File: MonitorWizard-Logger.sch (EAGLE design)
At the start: 40 parts, among them CON1 MICROSD, IC1 LD117AV33, J1 22-27-2041-04, J2 22-27-2041-04, J3 22-27-2041-04, U1 DHT22, U2 RFM69HW, U3 LTC3531, U4-NRF24L01 NRF24L01+-PCB-AERIAL, U6 ATMEGA328P-PU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

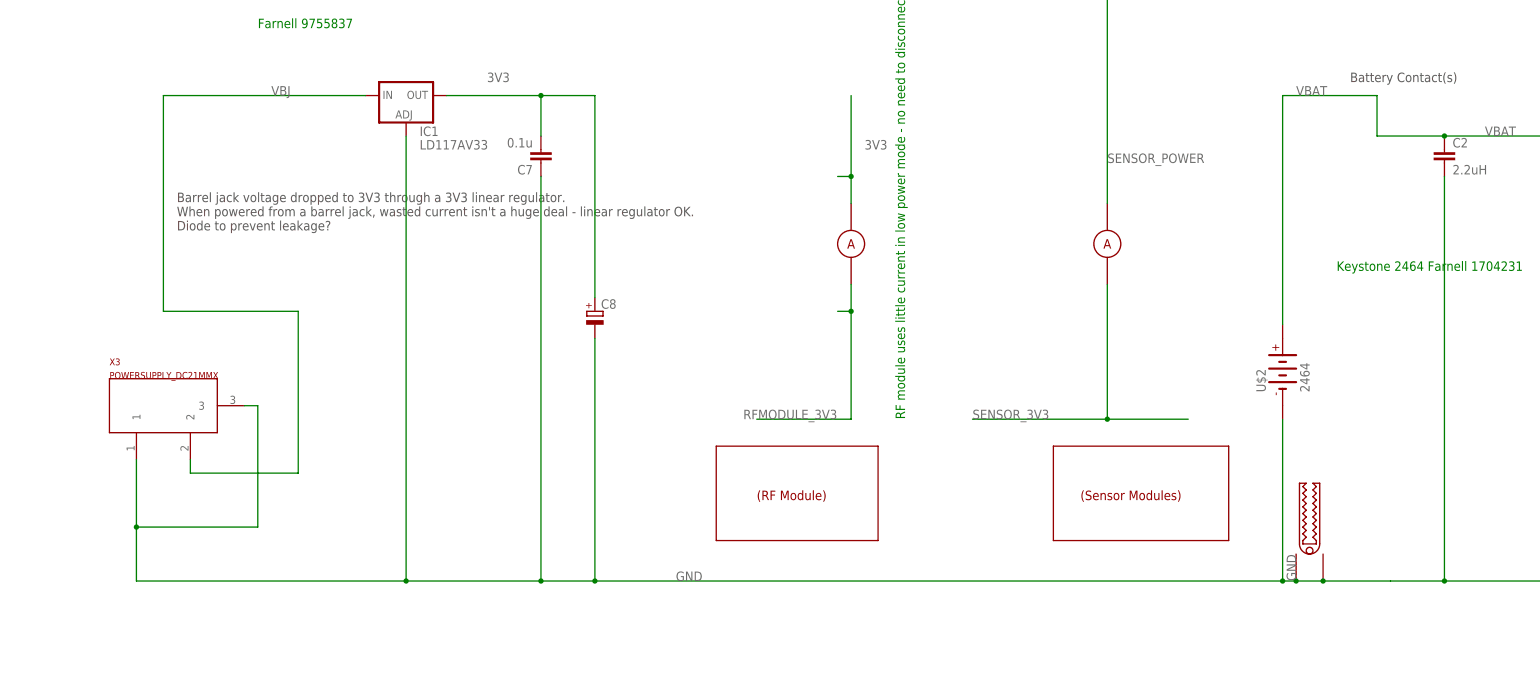
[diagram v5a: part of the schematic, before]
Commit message: Change to a better barrel jack footprint
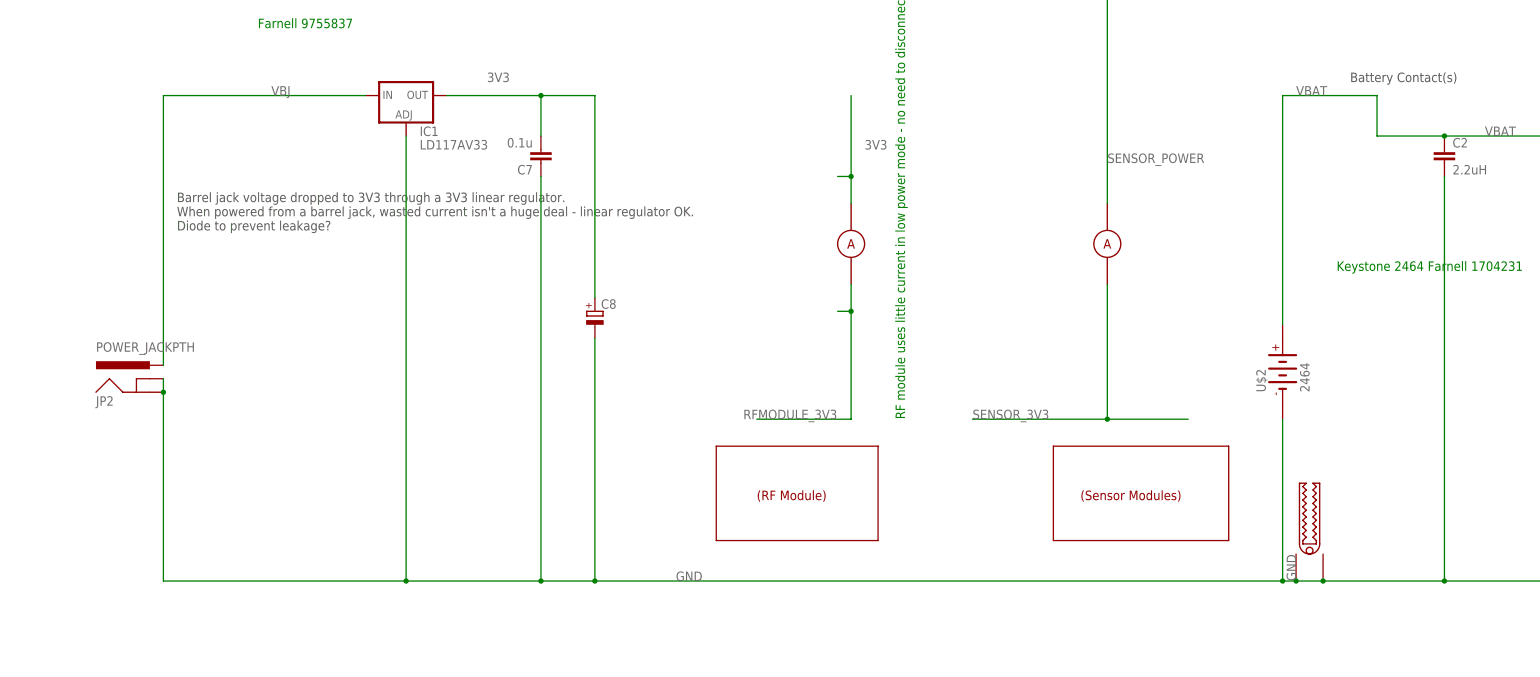
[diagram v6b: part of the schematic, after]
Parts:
- removed X3: POWERSUPPLY_DC21MMX, SmartPrj:POWERSUPPLY_DC21MMX
- added JP2: POWER_JACKPTH, SparkFun-Connectors:POWER_JACKPTH
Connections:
- net GND: now also JP2.GND, JP2.GNDBREAK; no longer X3.1, X3.3
- net VBJ: now also JP2.PWR; no longer X3.2
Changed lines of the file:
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@@
 <part name="AER" library="solpad" deviceset="LSP10" device=""/>
 <part name="GND" library="Probes" deviceset="ALLIGATOR" device=""/>
-<part name="X3" library="SmartPrj" deviceset="POWERSUPPLY_DC21MM" device="X"/>
 <part name="FD4" library="SmartPrj" deviceset="FIDUCIALMOUNT" device=""/>
 <part name="I_SENSE" library="Probes" deviceset="CURRENT_MEASURE" device="_0.4A"/>
@@
 <part name="C7" library="rcl" deviceset="C-EU" device="025-024X044" value="0.1u"/>
 <part name="C8" library="rcl" deviceset="CPOL-EU" device="E2.5-6"/>
+<part name="JP2" library="SparkFun-Connectors" deviceset="POWER_JACK" device="PTH"/>
 </parts>
 <sheets>
@@
 <instance part="AER" gate="1" x="408.94" y="-116.84" rot="R270"/>
 <instance part="GND" gate="G$1" x="525.78" y="-388.62" rot="R90"/>
-<instance part="X3" gate="G$1" x="309.88" y="-360.68" smashed="yes">
-<attribute name="NAME" x="299.72" y="-353.06" size="1.27" layer="94"/>
-<attribute name="VALUE" x="299.72" y="-355.6" size="1.27" layer="94"/>
-</instance>
 <instance part="FD4" gate="G$1" x="599.44" y="-88.9"/>
 <instance part="I_SENSE" gate="G$1" x="487.68" y="-330.2"/>
@@
 <instance part="C7" gate="G$1" x="381" y="-314.96" rot="R180"/>
 <instance part="C8" gate="G$1" x="391.16" y="-342.9"/>
+<instance part="JP2" gate="G$1" x="307.34" y="-360.68"/>
 </instances>
 <busses>
@@
 <net name="GND" class="2">
 <segment>
-<wire x1="528.32" y1="-393.7" x2="541.02" y2="-393.7" width="0.1524" layer="91"/>
+<wire x1="528.32" y1="-393.7" x2="551.18" y2="-393.7" width="0.1524" layer="91"/>
 <label x="406.4" y="-393.7" size="1.778" layer="95"/>
 <pinref part="GND" gate="G$1" pin="TOP"/>
@@
 <pinref part="GND" gate="G$1" pin="BTM"/>
 <junction x="528.32" y="-393.7"/>
-<pinref part="X3" gate="G$1" pin="3"/>
-<wire x1="325.12" y1="-360.68" x2="327.66" y2="-360.68" width="0.1524" layer="91"/>
-<wire x1="327.66" y1="-360.68" x2="327.66" y2="-383.54" width="0.1524" layer="91"/>
-<pinref part="X3" gate="G$1" pin="1"/>
-<wire x1="327.66" y1="-383.54" x2="304.8" y2="-383.54" width="0.1524" layer="91"/>
-<wire x1="304.8" y1="-383.54" x2="304.8" y2="-370.84" width="0.1524" layer="91"/>
-<wire x1="304.8" y1="-383.54" x2="304.8" y2="-393.7" width="0.1524" layer="91"/>
-<wire x1="304.8" y1="-393.7" x2="355.6" y2="-393.7" width="0.1524" layer="91"/>
-<junction x="304.8" y="-383.54"/>
+<wire x1="309.88" y1="-393.7" x2="355.6" y2="-393.7" width="0.1524" layer="91"/>
 <wire x1="355.6" y1="-393.7" x2="381" y2="-393.7" width="0.1524" layer="91"/>
 <wire x1="381" y1="-393.7" x2="391.16" y2="-393.7" width="0.1524" layer="91"/>
@@
 <wire x1="586.74" y1="-393.7" x2="551.18" y2="-393.7" width="0.1524" layer="91"/>
 <pinref part="R1" gate="G$1" pin="1"/>
-<wire x1="551.18" y1="-393.7" x2="541.02" y2="-393.7" width="0.1524" layer="91"/>
 <wire x1="612.14" y1="-373.38" x2="612.14" y2="-393.7" width="0.1524" layer="91"/>
 <wire x1="612.14" y1="-393.7" x2="586.74" y2="-393.7" width="0.1524" layer="91"/>
@@
 <wire x1="391.16" y1="-347.98" x2="391.16" y2="-393.7" width="0.1524" layer="91"/>
 <junction x="391.16" y="-393.7"/>
+<pinref part="JP2" gate="G$1" pin="GNDBREAK"/>
+<pinref part="JP2" gate="G$1" pin="GND"/>
+<wire x1="309.88" y1="-355.6" x2="309.88" y2="-358.14" width="0.1524" layer="91"/>
+<wire x1="309.88" y1="-358.14" x2="309.88" y2="-393.7" width="0.1524" layer="91"/>
+<junction x="309.88" y="-358.14"/>
 </segment>
 <segment>
@@
 <net name="VBJ" class="0">
 <segment>
-<pinref part="X3" gate="G$1" pin="2"/>
-<wire x1="314.96" y1="-370.84" x2="314.96" y2="-373.38" width="0.1524" layer="91"/>
-<wire x1="314.96" y1="-373.38" x2="335.28" y2="-373.38" width="0.1524" layer="91"/>
 <label x="330.2" y="-302.26" size="1.778" layer="95"/>
-<wire x1="335.28" y1="-373.38" x2="335.28" y2="-342.9" width="0.1524" layer="91"/>
-<wire x1="335.28" y1="-342.9" x2="309.88" y2="-342.9" width="0.1524" layer="91"/>
-<wire x1="309.88" y1="-342.9" x2="309.88" y2="-302.26" width="0.1524" layer="91"/>
+<wire x1="309.88" y1="-353.06" x2="309.88" y2="-302.26" width="0.1524" layer="91"/>
 <wire x1="309.88" y1="-302.26" x2="347.98" y2="-302.26" width="0.1524" layer="91"/>
 <pinref part="IC1" gate="G$1" pin="IN"/>
-</segment>
-</net>
+<pinref part="JP2" gate="G$1" pin="PWR"/>
+</segment>
+</net>

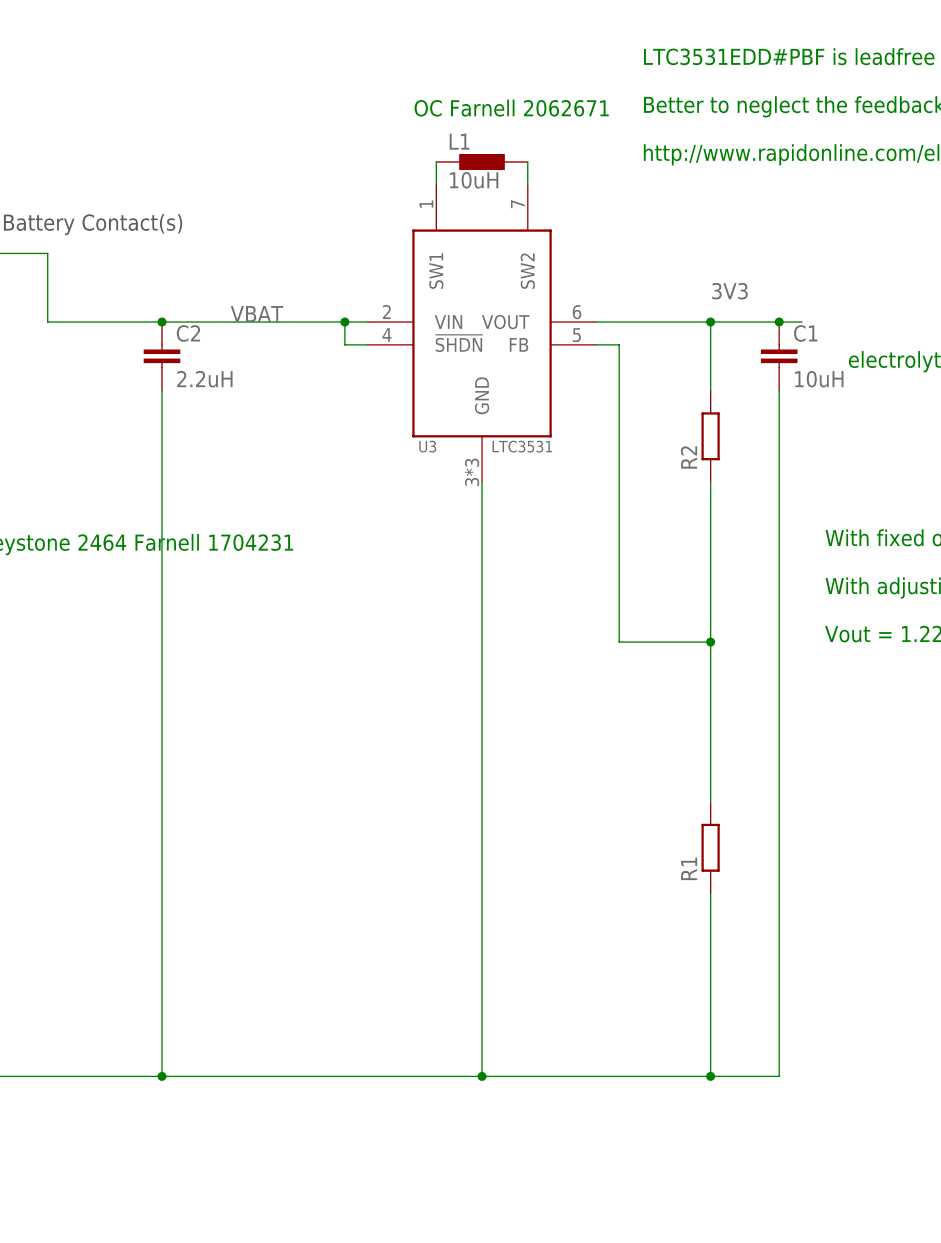
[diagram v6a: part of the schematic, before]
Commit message: Change footprint for LTC3531
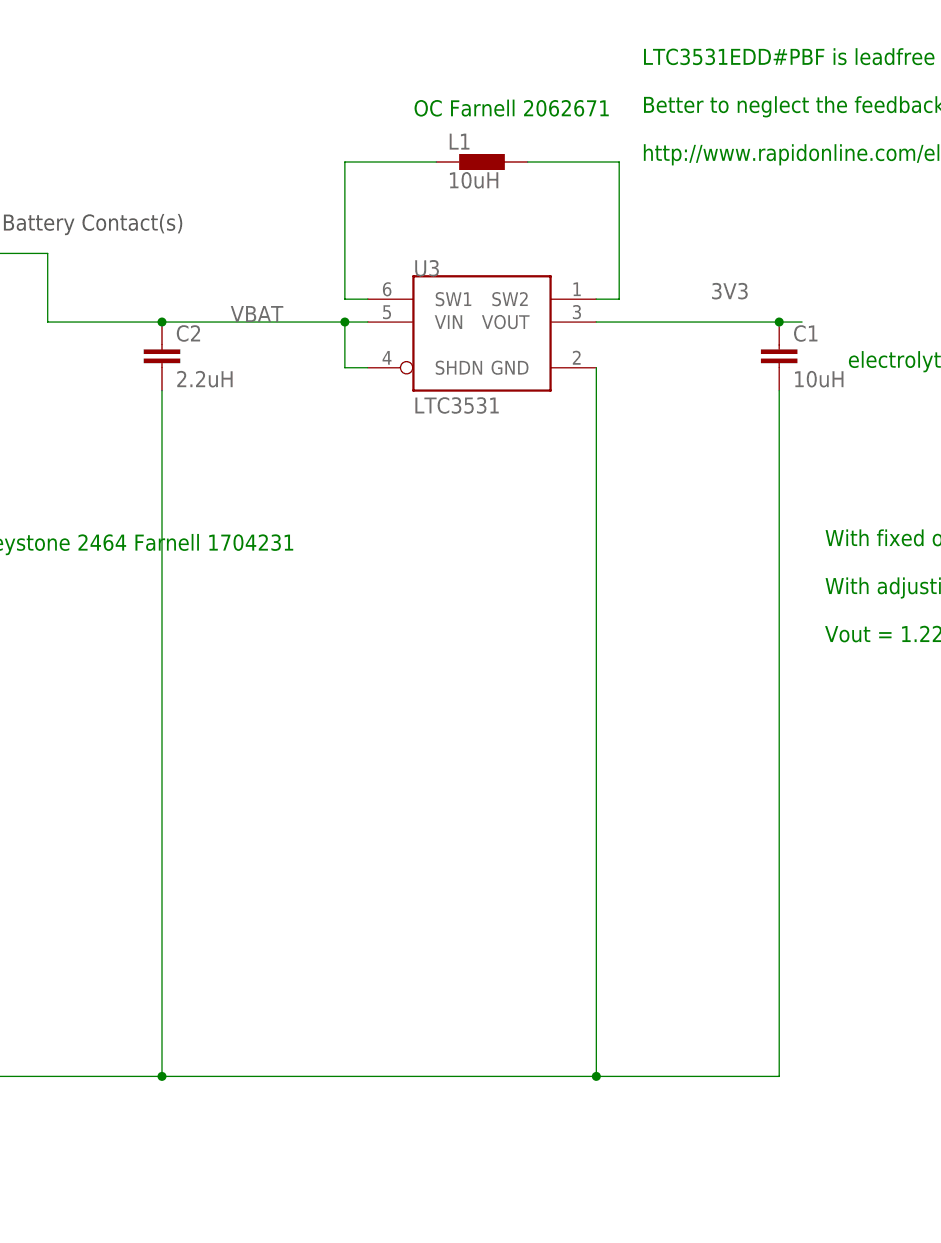
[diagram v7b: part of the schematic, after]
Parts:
- removed R1, R2: (no value), resistor:R-EU_0207/10
- U3: device exported-lbrlinear-sen:LTC3531 -> custom:LTC3531
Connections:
- removed net N$3: R1.2, R2.1, U3.FB
- net 3V3: no longer R2.2
- net GND: no longer R1.1
- net VBAT: now also U3.SHDN; no longer U3.!SHDN
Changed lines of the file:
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@@
 <part name="R3" library="resistor" deviceset="R-EU_" device="0207/10" value="10K"/>
 <part name="U2" library="SparkFun-RF" deviceset="RFM69H" device="W"/>
-<part name="U3" library="exported-lbrlinear-sen" deviceset="LTC3531" device=""/>
 <part name="L1" library="InductorsThru" deviceset="MURATA-1100R" device="" value="10uH"/>
-<part name="R1" library="resistor" deviceset="R-EU_" device="0207/10"/>
-<part name="R2" library="resistor" deviceset="R-EU_" device="0207/10"/>
 <part name="C1" library="rcl" deviceset="C-EU" device="025-024X044" value="10uH"/>
 <part name="C2" library="rcl" deviceset="C-EU" device="025-024X044" value="2.2uH"/>
@@
 <part name="C8" library="rcl" deviceset="CPOL-EU" device="E2.5-6"/>
 <part name="JP2" library="SparkFun-Connectors" deviceset="POWER_JACK" device="PTH"/>
+<part name="U3" library="custom" deviceset="LTC3531" device=""/>
 </parts>
 <sheets>
@@
 <instance part="R3" gate="G$1" x="119.38" y="-355.6" rot="R90"/>
 <instance part="U2" gate="G$1" x="383.54" y="-109.22"/>
-<instance part="U3" gate="G$1" x="586.74" y="-309.88"/>
 <instance part="L1" gate="G$1" x="586.74" y="-292.1"/>
-<instance part="R1" gate="G$1" x="612.14" y="-368.3" rot="R90"/>
-<instance part="R2" gate="G$1" x="612.14" y="-322.58" rot="R90"/>
 <instance part="C1" gate="G$1" x="619.76" y="-312.42"/>
 <instance part="C2" gate="G$1" x="551.18" y="-312.42"/>
@@
 <instance part="C8" gate="G$1" x="391.16" y="-342.9"/>
 <instance part="JP2" gate="G$1" x="307.34" y="-360.68"/>
+<instance part="U3" gate="G$1" x="584.2" y="-312.42"/>
 </instances>
 <busses>
@@
 <wire x1="355.6" y1="-309.88" x2="355.6" y2="-393.7" width="0.1524" layer="91"/>
 <junction x="355.6" y="-393.7"/>
-<pinref part="U3" gate="G$1" pin="GND"/>
-<wire x1="586.74" y1="-327.66" x2="586.74" y2="-393.7" width="0.1524" layer="91"/>
-<wire x1="586.74" y1="-393.7" x2="551.18" y2="-393.7" width="0.1524" layer="91"/>
-<pinref part="R1" gate="G$1" pin="1"/>
-<wire x1="612.14" y1="-373.38" x2="612.14" y2="-393.7" width="0.1524" layer="91"/>
-<wire x1="612.14" y1="-393.7" x2="586.74" y2="-393.7" width="0.1524" layer="91"/>
-<junction x="586.74" y="-393.7"/>
+<wire x1="599.44" y1="-393.7" x2="551.18" y2="-393.7" width="0.1524" layer="91"/>
+<wire x1="619.76" y1="-393.7" x2="599.44" y2="-393.7" width="0.1524" layer="91"/>
+<junction x="599.44" y="-393.7"/>
 <pinref part="C2" gate="G$1" pin="2"/>
 <wire x1="551.18" y1="-317.5" x2="551.18" y2="-393.7" width="0.1524" layer="91"/>
 <junction x="551.18" y="-393.7"/>
 <pinref part="C1" gate="G$1" pin="2"/>
-<wire x1="612.14" y1="-393.7" x2="619.76" y2="-393.7" width="0.1524" layer="91"/>
 <wire x1="619.76" y1="-393.7" x2="619.76" y2="-317.5" width="0.1524" layer="91"/>
-<junction x="612.14" y="-393.7"/>
 <pinref part="IC1" gate="G$1" pin="ADJ"/>
 <pinref part="U$2" gate="G$1" pin="-"/>
@@
 <wire x1="309.88" y1="-358.14" x2="309.88" y2="-393.7" width="0.1524" layer="91"/>
 <junction x="309.88" y="-358.14"/>
+<pinref part="U3" gate="G$1" pin="GND"/>
+<wire x1="599.44" y1="-393.7" x2="599.44" y2="-314.96" width="0.1524" layer="91"/>
 </segment>
 <segment>
@@
 <segment>
 <label x="523.24" y="-302.26" size="1.778" layer="95"/>
-<pinref part="U3" gate="G$1" pin="VIN"/>
 <wire x1="574.04" y1="-309.88" x2="571.5" y2="-309.88" width="0.1524" layer="91"/>
 <wire x1="571.5" y1="-309.88" x2="551.18" y2="-309.88" width="0.1524" layer="91"/>
@@
 <wire x1="538.48" y1="-302.26" x2="520.7" y2="-302.26" width="0.1524" layer="91"/>
 <label x="558.8" y="-309.88" size="1.778" layer="95"/>
-<pinref part="U3" gate="G$1" pin="!SHDN"/>
-<wire x1="574.04" y1="-312.42" x2="571.5" y2="-312.42" width="0.1524" layer="91"/>
-<wire x1="571.5" y1="-312.42" x2="571.5" y2="-309.88" width="0.1524" layer="91"/>
+<wire x1="571.5" y1="-314.96" x2="571.5" y2="-309.88" width="0.1524" layer="91"/>
 <junction x="571.5" y="-309.88"/>
 <pinref part="C2" gate="G$1" pin="1"/>
@@
 <wire x1="520.7" y1="-345.44" x2="520.7" y2="-302.26" width="0.1524" layer="91"/>
 <pinref part="U$2" gate="G$1" pin="+"/>
+<pinref part="U3" gate="G$1" pin="VIN"/>
+<pinref part="U3" gate="G$1" pin="SHDN"/>
+<wire x1="574.04" y1="-314.96" x2="571.5" y2="-314.96" width="0.1524" layer="91"/>
 </segment>
 </net>
@@
 </segment>
 <segment>
-<pinref part="U3" gate="G$1" pin="VOUT"/>
-<wire x1="599.44" y1="-309.88" x2="612.14" y2="-309.88" width="0.1524" layer="91"/>
+<wire x1="599.44" y1="-309.88" x2="619.76" y2="-309.88" width="0.1524" layer="91"/>
 <label x="612.14" y="-307.34" size="1.778" layer="95"/>
-<pinref part="R2" gate="G$1" pin="2"/>
-<wire x1="612.14" y1="-309.88" x2="619.76" y2="-309.88" width="0.1524" layer="91"/>
 <wire x1="619.76" y1="-309.88" x2="622.3" y2="-309.88" width="0.1524" layer="91"/>
-<wire x1="612.14" y1="-317.5" x2="612.14" y2="-309.88" width="0.1524" layer="91"/>
-<junction x="612.14" y="-309.88"/>
 <pinref part="C1" gate="G$1" pin="1"/>
 <junction x="619.76" y="-309.88"/>
+<pinref part="U3" gate="G$1" pin="VOUT"/>
 </segment>
 <segment>
@@
 <net name="N$1" class="0">
 <segment>
+<pinref part="L1" gate="G$1" pin="2"/>
+<wire x1="591.82" y1="-292.1" x2="601.98" y2="-292.1" width="0.1524" layer="91"/>
 <pinref part="U3" gate="G$1" pin="SW2"/>
-<pinref part="L1" gate="G$1" pin="2"/>
-<wire x1="591.82" y1="-292.1" x2="591.82" y2="-294.64" width="0.1524" layer="91"/>
+<wire x1="601.98" y1="-292.1" x2="601.98" y2="-307.34" width="0.1524" layer="91"/>
+<wire x1="601.98" y1="-307.34" x2="599.44" y2="-307.34" width="0.1524" layer="91"/>
 </segment>
 </net>
 <net name="N$2" class="0">
 <segment>
+<pinref part="L1" gate="G$1" pin="1"/>
 <pinref part="U3" gate="G$1" pin="SW1"/>
-<pinref part="L1" gate="G$1" pin="1"/>
-<wire x1="581.66" y1="-292.1" x2="581.66" y2="-294.64" width="0.1524" layer="91"/>
-</segment>
-</net>
-<net name="N$3" class="0">
-<segment>
-<pinref part="R1" gate="G$1" pin="2"/>
-<pinref part="R2" gate="G$1" pin="1"/>
-<wire x1="612.14" y1="-327.66" x2="612.14" y2="-345.44" width="0.1524" layer="91"/>
-<wire x1="612.14" y1="-345.44" x2="612.14" y2="-363.22" width="0.1524" layer="91"/>
-<wire x1="612.14" y1="-345.44" x2="601.98" y2="-345.44" width="0.1524" layer="91"/>
-<wire x1="601.98" y1="-345.44" x2="601.98" y2="-312.42" width="0.1524" layer="91"/>
-<junction x="612.14" y="-345.44"/>
-<pinref part="U3" gate="G$1" pin="FB"/>
-<wire x1="601.98" y1="-312.42" x2="599.44" y2="-312.42" width="0.1524" layer="91"/>
-</segment>
-</net>
+<wire x1="574.04" y1="-307.34" x2="571.5" y2="-307.34" width="0.1524" layer="91"/>
+<wire x1="571.5" y1="-307.34" x2="571.5" y2="-292.1" width="0.1524" layer="91"/>
+<wire x1="571.5" y1="-292.1" x2="581.66" y2="-292.1" width="0.1524" layer="91"/>
+</segment>
+</net>
